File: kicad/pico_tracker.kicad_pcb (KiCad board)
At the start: 2 copper layers, 92.9 x 125.4 mm, 30 parts, among them J1 MIDI_OUT, J10 DclassAMP, J2 MIDI_IN, J3 MIDI_IN_A_B_VCC, J4 MIDI_IN_A_B_DATA, J5 MIDI_OUT_A_B_VCC, J6 MIDI_OUT_A_B_DATA, J7 DISPLAY, J8 SDCARD, J9 KILL_SWITCH, SW1 SW_PG1350, SW2 SW_PG1350, SW3 SW_PG1350, SW4 SW_PG1350, SW5 SW_PG1350, SW6 SW_PG1350, SW7 SW_PG1350, SW8 SW_PG1350, SW9 SW_PG1350, U1 Pico, U2 6N138, U3 PCM5102_Module

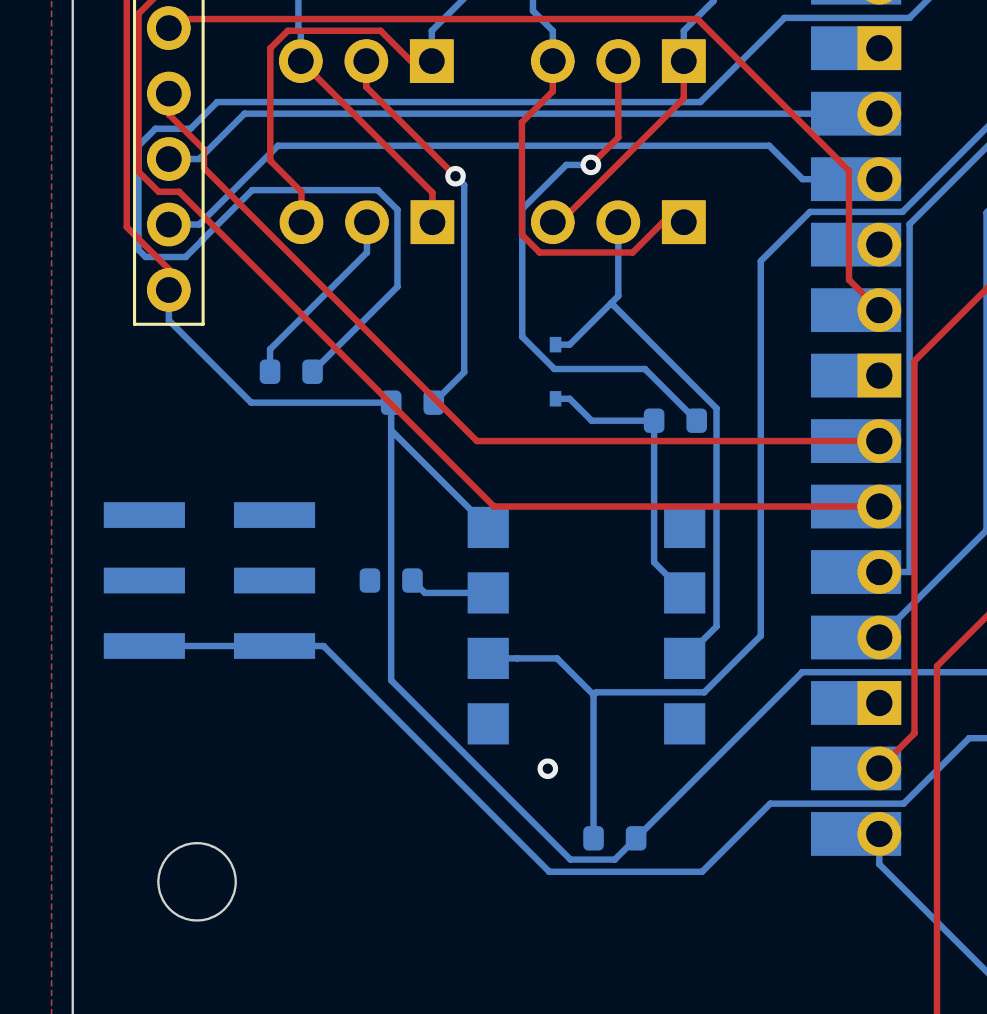
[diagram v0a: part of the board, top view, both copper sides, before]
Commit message: switch to tht, update parts links with estimated prices
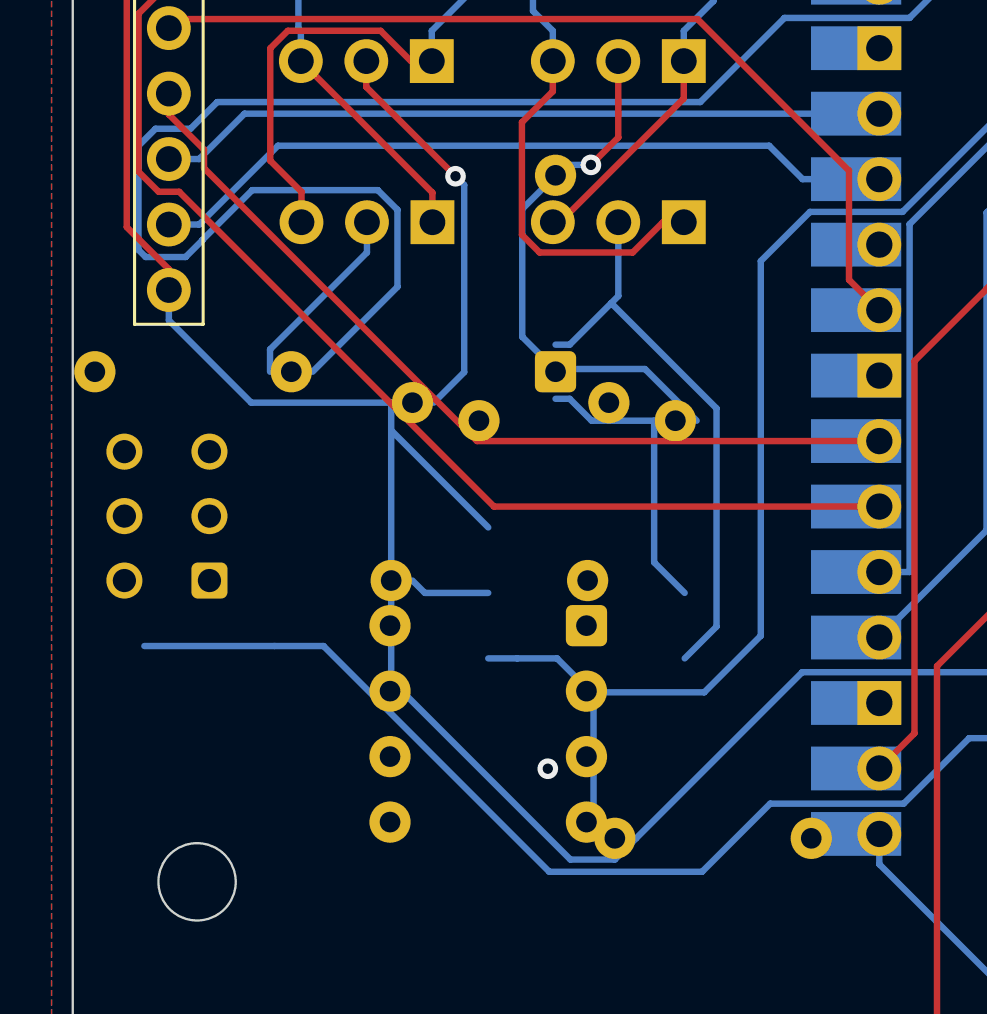
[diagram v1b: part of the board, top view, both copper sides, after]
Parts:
- D1: footprint Diode_SMD:D_SOD-323 -> Diode_THT:D_DO-35_SOD27_P7.62mm_Horizontal
- J9: footprint Connector_PinHeader_2.54mm:PinHeader_2x03_P2.54mm_Vertical_SMD -> Button_Switch_THT:SW_CK_JS202011AQN_DPDT_Angled
- R1, R2, R3, R4, R5: footprint Resistor_SMD:R_0603_1608Metric -> Resistor_THT:R_Axial_DIN0207_L6.3mm_D2.5mm_P7.62mm_Horizontal
- U2: footprint Package_DIP:DIP-8_W7.62mm_SMDSocket_SmallPads -> Package_DIP:DIP-8_W7.62mm
- turned J9 to 90 degrees
